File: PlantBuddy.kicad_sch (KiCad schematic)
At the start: 42 parts, among them J1 USB_C_Receptacle_USB2.0, J2 C+, J3 C-, J4 Expansion Header, Q1 DMG1012T, SW1 SW_Push, U1 LTR-303ALS-01, U2 SHTC3, U3 ESP32-S3-WROOM-1-N8R8, U4 BQ24072RGT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

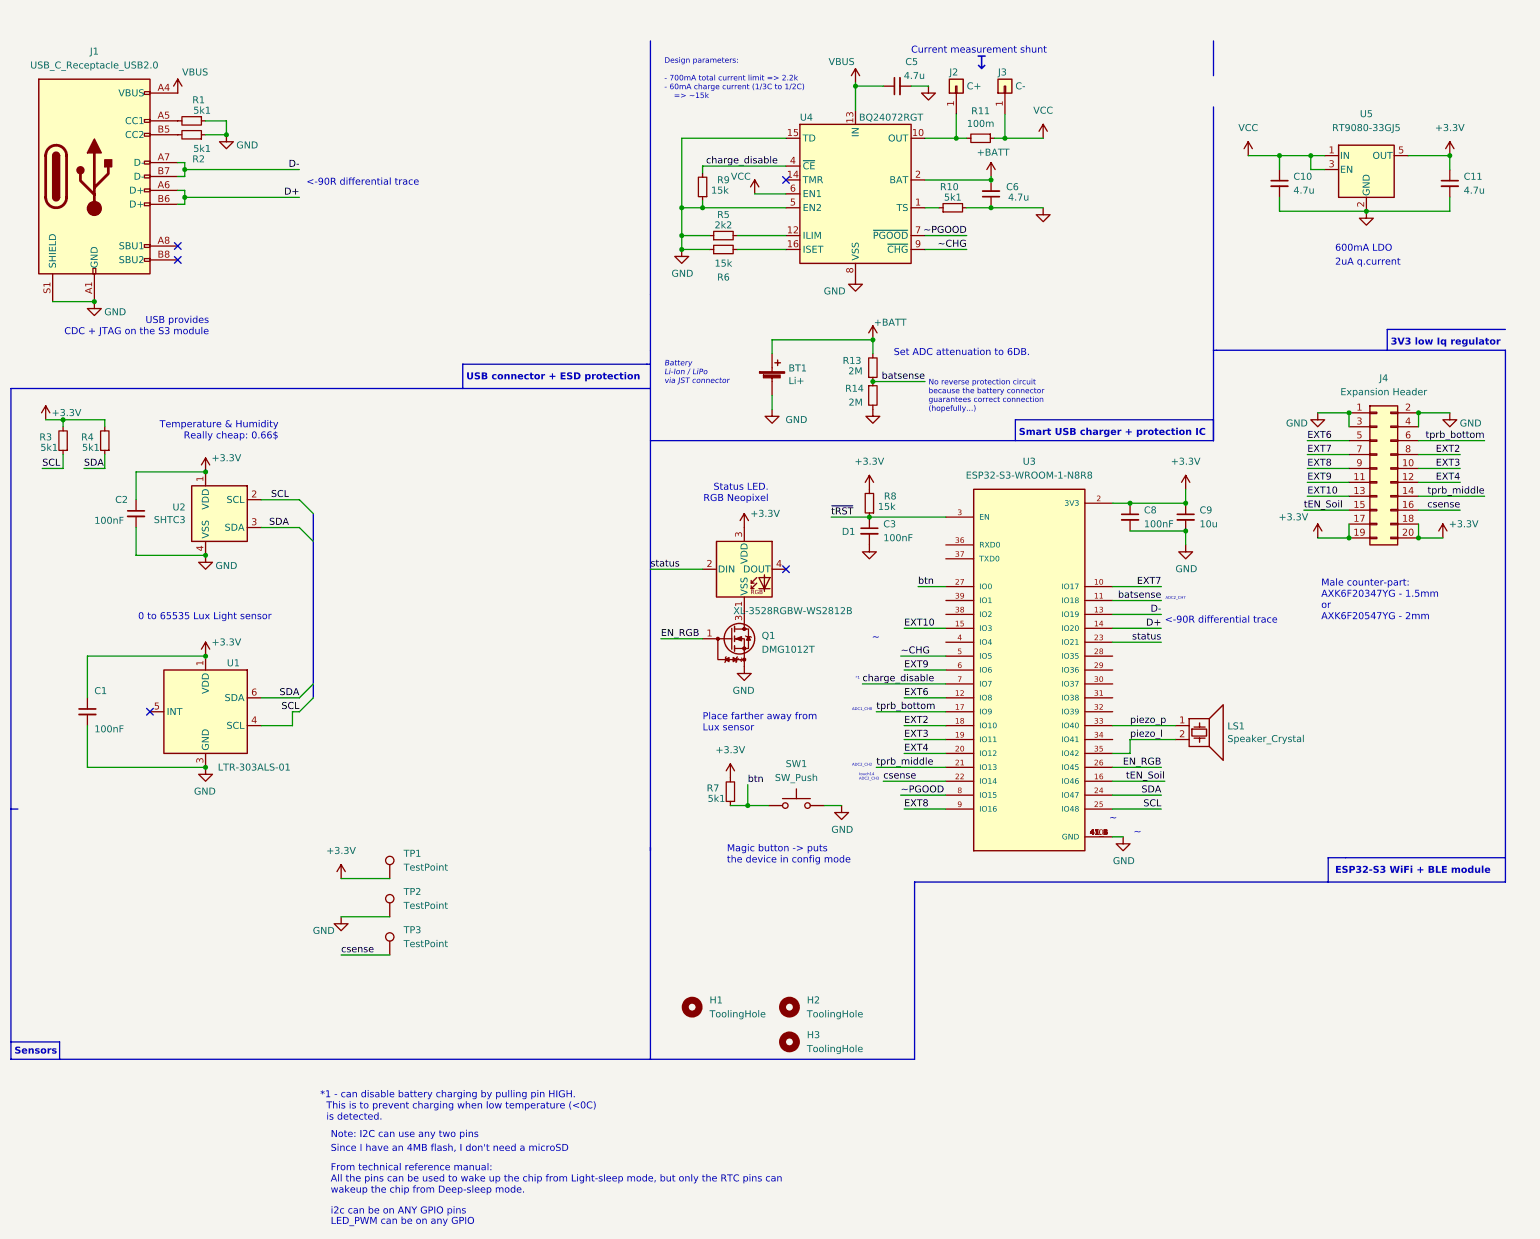
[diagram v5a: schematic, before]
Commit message: Fixed board after first batch arrived. Changed connector to FFC.
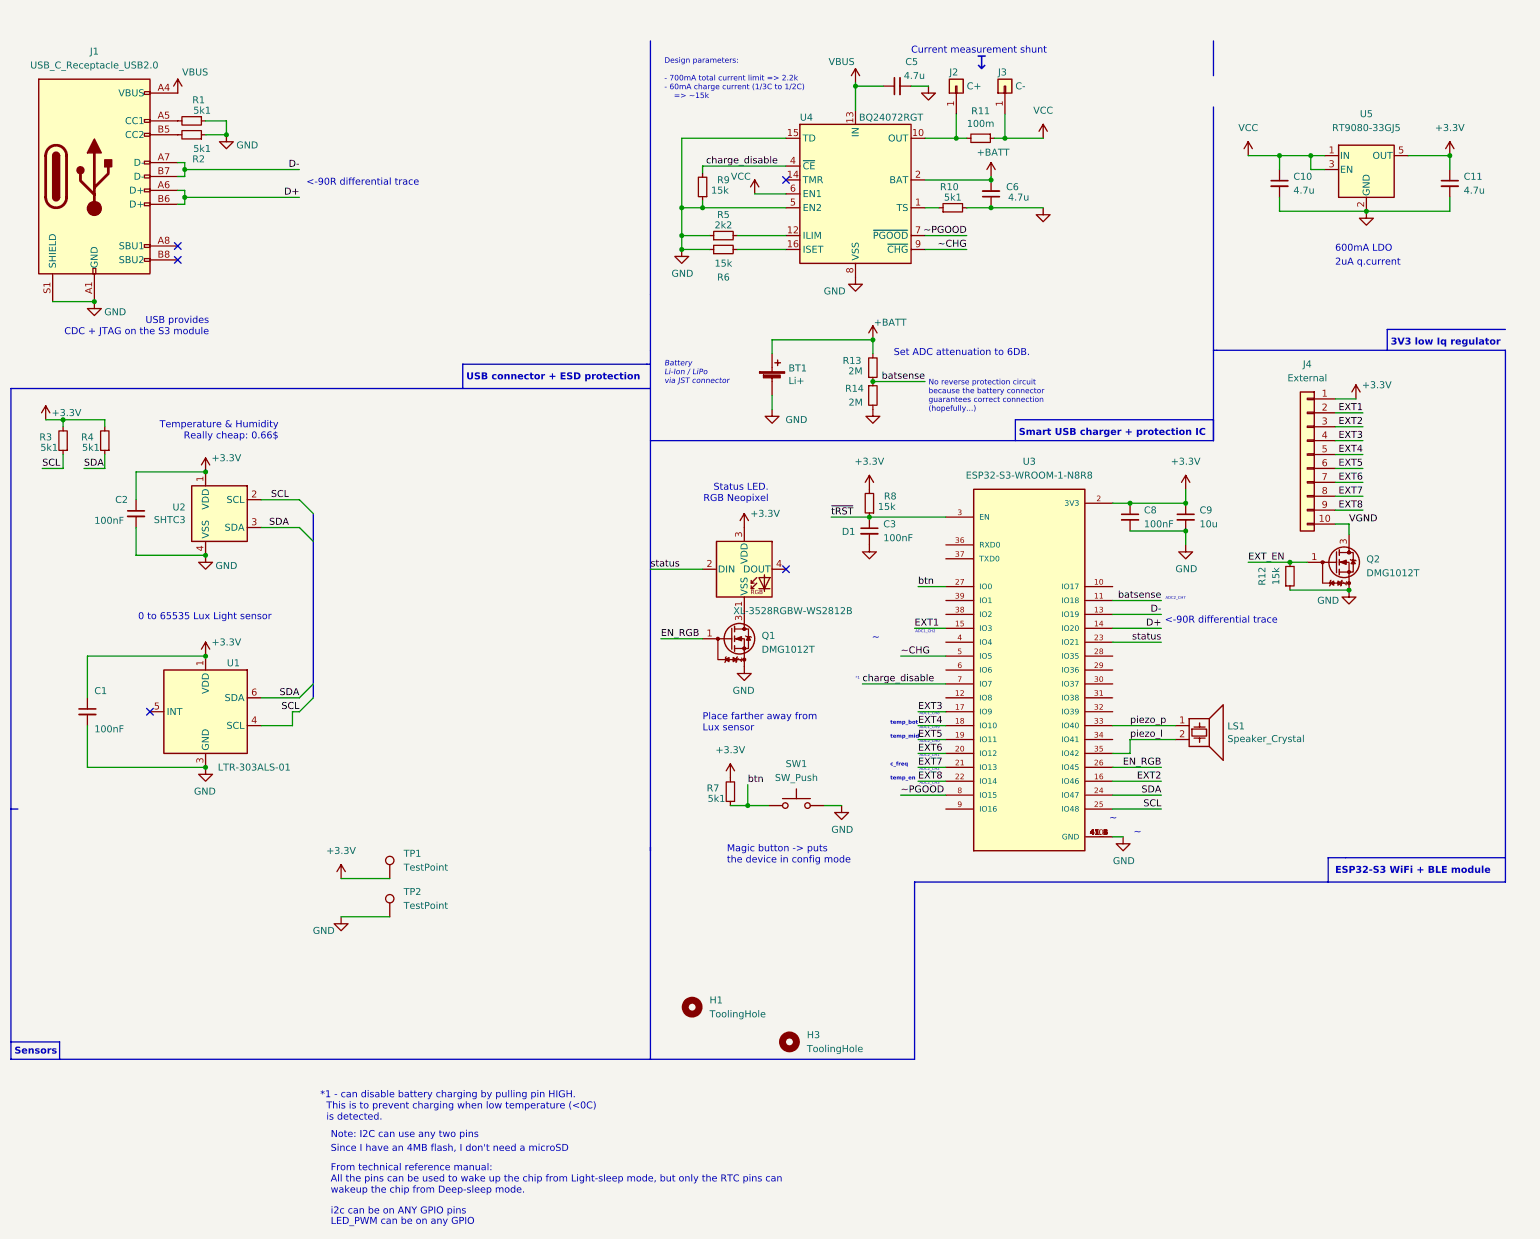
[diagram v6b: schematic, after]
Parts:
- removed H2: ToolingHole, Tooling:JLCPCB_Tooling_hole, symbol Mechanical:MountingHole
- removed J4: Expansion Header, Mezzanine-pb:AXK5F20547YG, symbol Connector_Generic:Conn_02x10_Odd_Even
- removed TP3: TestPoint, TestPoint:TestPoint_Pad_D2.0mm, symbol Connector:TestPoint
- added J4: External, Connector_FFC-FPC:Hirose_FH12-10S-0.5SH_1x10-1MP_P0.50mm_Horizontal, symbol Connector_Generic:Conn_01x10
- added Q2: DMG1012T, Package_TO_SOT_SMD:SOT-523, symbol Transistor_FET:DMG1012T
- added R12: 15k, Resistor_SMD:R_0603_1608Metric, symbol Device:R_Small
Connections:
- net csense is gone; now on net EXT8: U3.22 (IO14)
- net tEN_Soil is gone; now on net EXT2: U3.16 (IO46)
- net tprb_bottom is gone; now on net EXT3: U3.17 (IO9)
- net tprb_middle is gone; now on net EXT7: U3.21 (IO13)
- net +3V3: now also J4.1 (Pin_1)
- net EXT2: now also J4.3 (Pin_3); no longer U3.18 (IO10)
- net EXT3: now also J4.4 (Pin_4); no longer U3.19 (IO11)
- net EXT4: now also U3.18 (IO10), J4.5 (Pin_5); no longer U3.20 (IO12)
- net EXT6: now also U3.20 (IO12), J4.7 (Pin_7); no longer U3.12 (IO8)
- net EXT7: now also J4.8 (Pin_8); no longer U3.10 (IO17)
- net EXT8: now also J4.9 (Pin_9); no longer U3.9 (IO16)
- net GND: now also Q2.2 (S), R12.1
- net EXT10 renamed EXT1
- net EXT1: now also J4.2 (Pin_2)
- net EXT9: no longer names the net of U3.6 (IO6)
- new net EXT5: J4.6 (Pin_6), U3.19 (IO11)
- new net EXT_EN: Q2.1 (G), R12.2
- new net VGND: J4.10 (Pin_10), Q2.3 (D)
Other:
- note added: "ADC1_CH2"
- note added: "ADC1_CH9"
- note added: "ADC2_CH0"
- note added: "ADC2_CH1"
- note added: "ADC2_CH3"
- note added: "c_freq"
- note added: "temp_bot"
- note added: "temp_en"
- note added: "temp_mid"
- note removed: "Male counter-part: AXK6F20347YG - 1.5mm or AXK6F20547YG - 2mm"
- note removed: "touch14 ADC2_CH3"

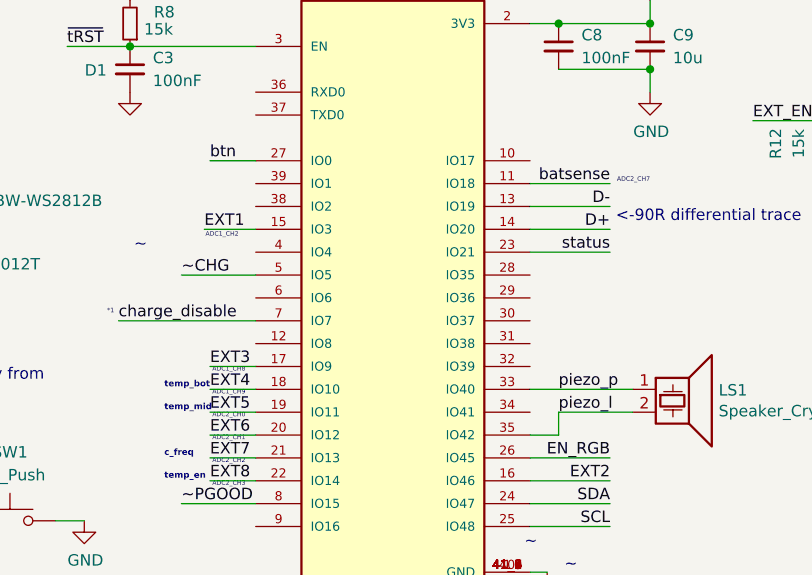
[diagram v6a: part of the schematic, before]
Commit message: Moved temp mid to ADC1_CH8 & batsense to ADC1_CH7. To note: only ADC1 can be used if WiFi is enabled!
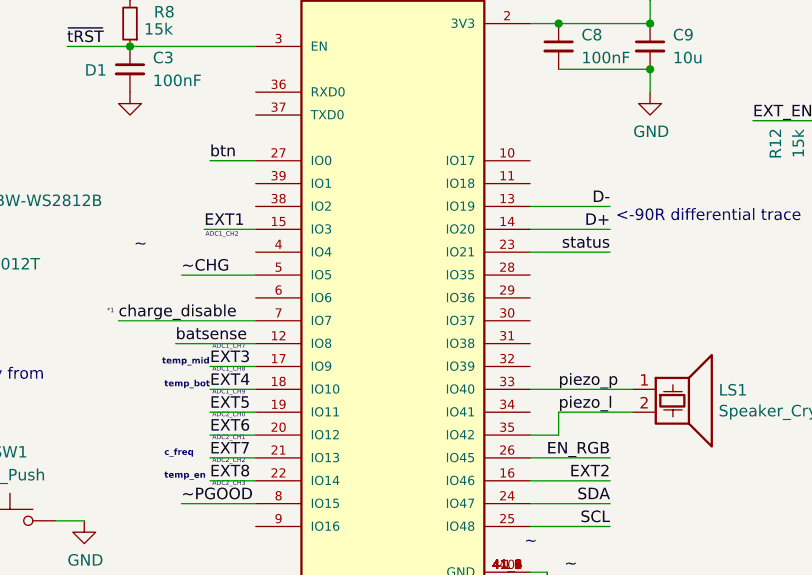
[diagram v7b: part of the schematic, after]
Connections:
- net batsense: now also U3.12 (IO8); no longer U3.11 (IO18)
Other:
- note added: "ADC1_CH7"
- note removed: "ADC2_CH7"
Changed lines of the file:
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@@
-    (stroke (width 0) (type default) (color 0 0 0 0))
-  )
-  (wire (pts (xy 222.25 114.3) (xy 213.36 114.3))
     (stroke (width 0) (type default) (color 0 0 0 0))
   )
@@
   )
   (wire (pts (xy 130.81 121.285) (xy 138.43 121.285))
+    (stroke (width 0) (type default) (color 0 0 0 0))
+  )
+  (wire (pts (xy 173.99 132.08) (xy 182.88 132.08))
     (stroke (width 0) (type default) (color 0 0 0 0))
   )
@@
   (text "i2c can be on ANY GPIO pins" (at 70.485 226.695 0)
     (effects (font (size 1.27 1.27)) (justify left bottom))
+  )
+  (text "ADC1_CH7" (at 178.054 132.842 0)
+    (effects (font (size 0.5 0.5)) (justify left bottom))
   )
   (text "From technical reference manual:\nAll the pins can be used to wake up the chip from Light-sleep mode, but only the RTC pins can\nwakeup the chip from Deep-sleep mode."
@@
     (effects (font (size 1.27 1.27)) (justify left bottom))
   )
-  (text "ADC2_CH7" (at 226.695 114.3 180)
-    (effects (font (size 0.5 0.5)) (justify right bottom))
-  )
   (text "Status LED.\nRGB Neopixel" (at 150.495 96.52 180)
     (effects (font (size 1.27 1.27)) (justify right bottom))
@@
     (effects (font (size 1 1)) (justify left bottom))
   )
-  (text "temp_mid" (at 172.72 139.7 0)
+  (text "temp_mid" (at 172.466 134.62 0)
     (effects (font (size 0.7 0.7) (thickness 0.14) bold) (justify left bottom))
   )
@@
     (effects (font (size 1.27 1.27)) (justify left bottom))
   )
+  (label "batsense" (at 173.99 132.08 0)
+    (effects (font (size 1.27 1.27)) (justify left bottom))
+  )
   (label "status" (at 222.25 121.92 180)
     (effects (font (size 1.27 1.27)) (justify right bottom))
   )
-  (label "batsense" (at 222.25 114.3 180)
-    (effects (font (size 1.27 1.27)) (justify right bottom))
-  )

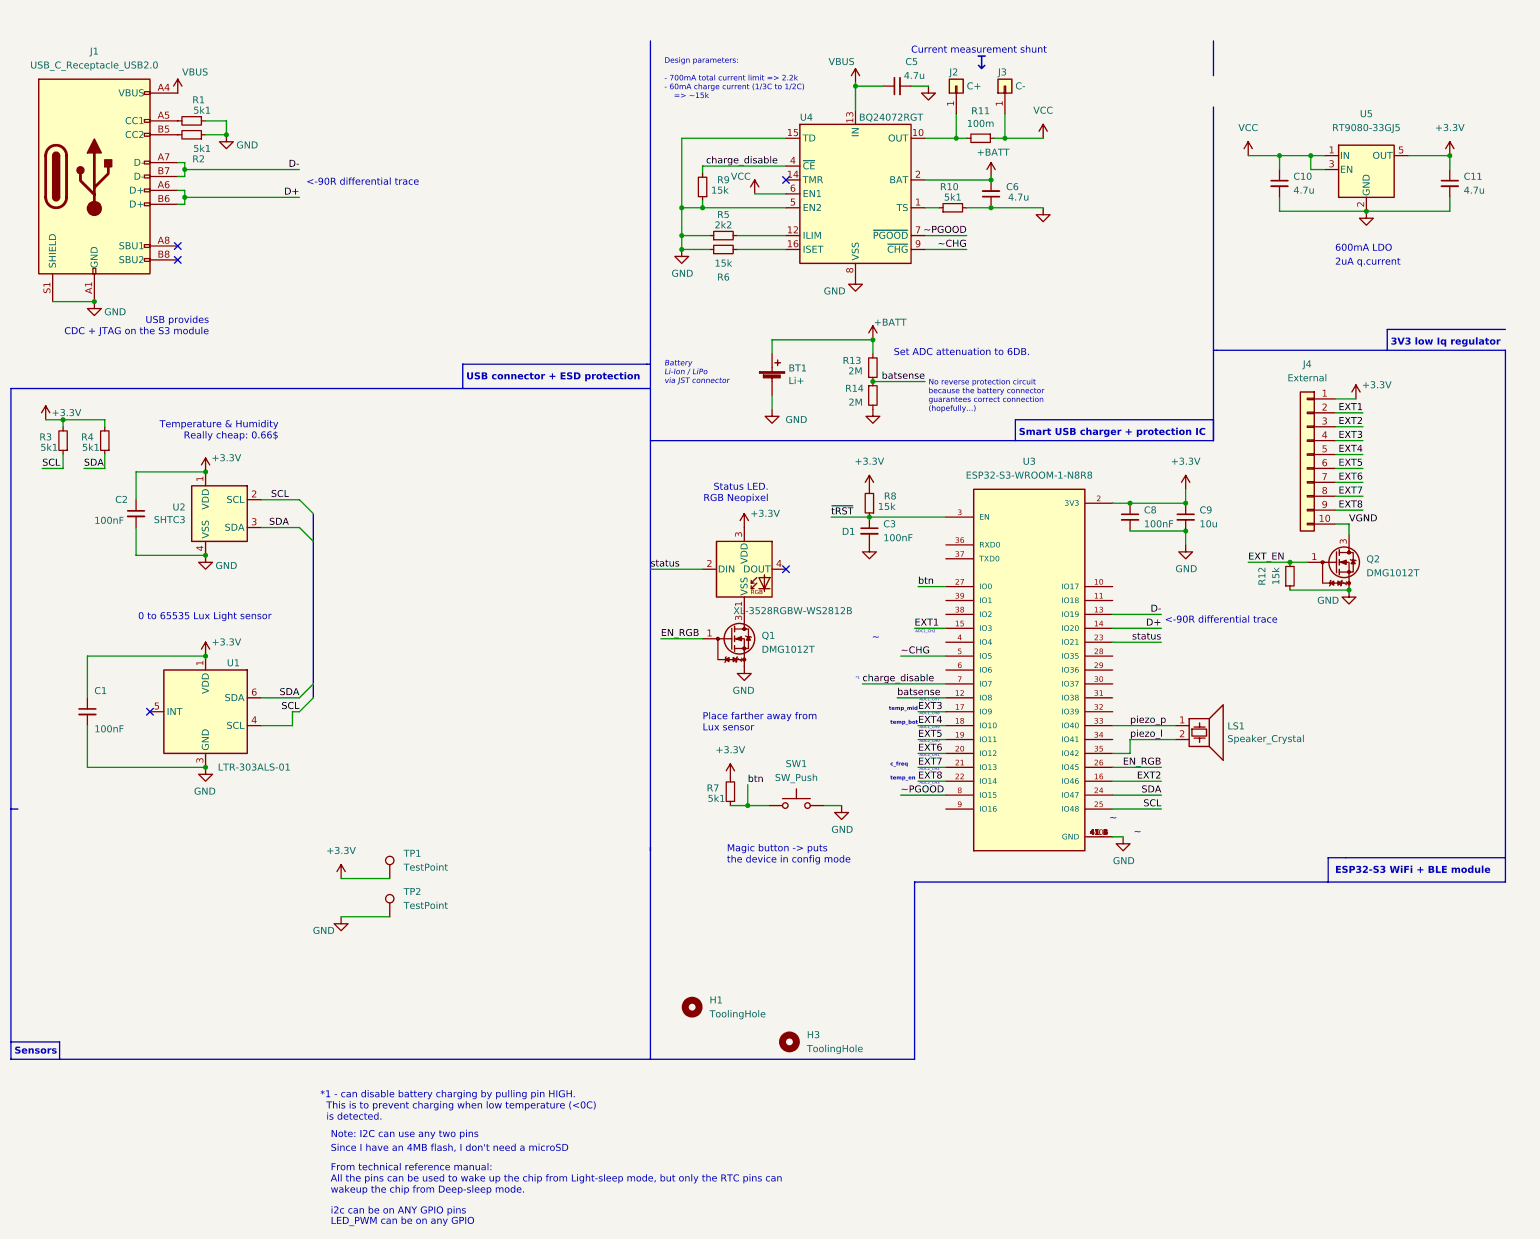
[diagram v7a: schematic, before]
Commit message: Added power distribution switch for external connector
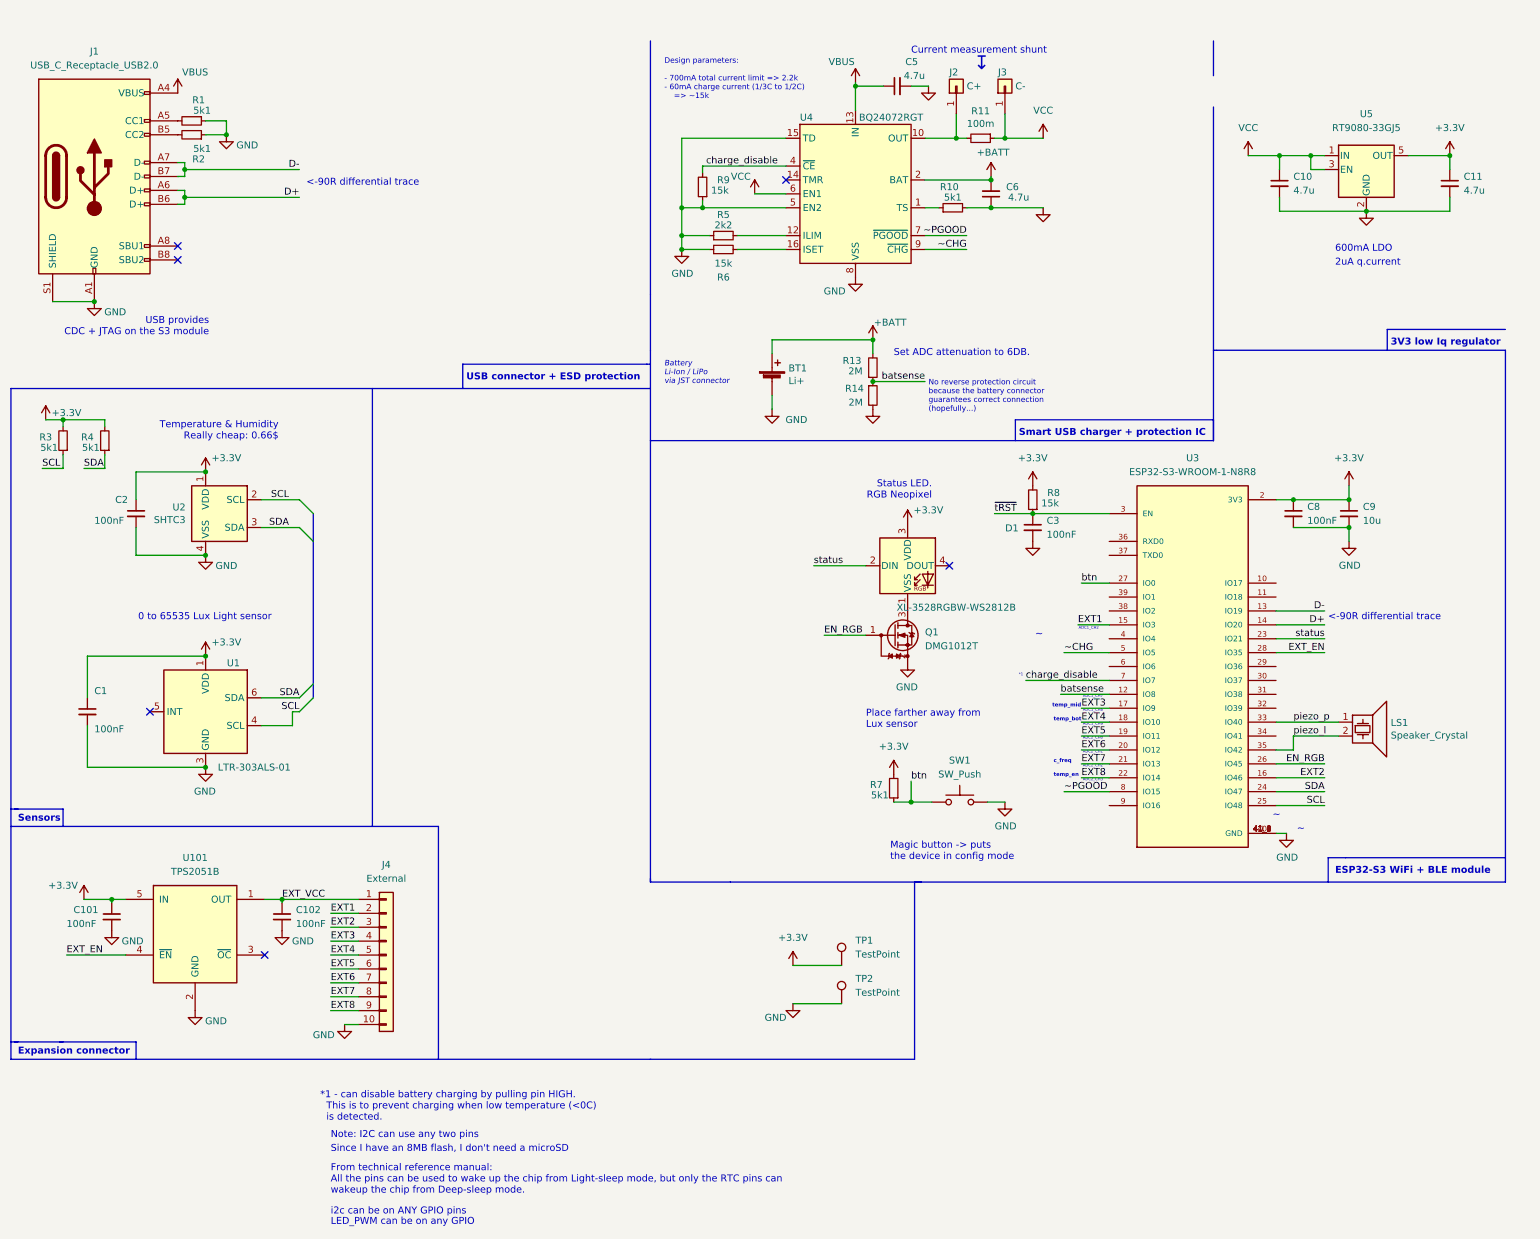
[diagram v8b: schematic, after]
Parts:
- removed H1, H3: ToolingHole, Tooling:JLCPCB_Tooling_hole, symbol Mechanical:MountingHole
- removed Q2: DMG1012T, Package_TO_SOT_SMD:SOT-523, symbol Transistor_FET:DMG1012T
- removed R12: 15k, Resistor_SMD:R_0603_1608Metric, symbol Device:R_Small
- added C101, C102: 100nF, Capacitor_SMD:C_0402_1005Metric, symbol Device:C_Small
- added U101: TPS2051B, Package_TO_SOT_SMD:SOT-23-5, symbol tps2051:TPS2051B
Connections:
- net VGND is gone; now on net GND: J4.10 (Pin_10)
- net +3V3: now also C101.1, U101.5 (IN); no longer J4.1 (Pin_1)
- net EXT_EN: now also U3.28 (IO35), U101.4 (~{EN})
- net GND: now also C101.2, C102.2, U101.2 (GND)
- new net EXT_VCC: C102.1, J4.1 (Pin_1), U101.1 (OUT)
- no-connect marks 5 -> 6
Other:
- note added: "Expansion connector"
- note added: "Since I have an 8MB flash, I don't need a microSD"
- note removed: "Since I have an 4MB flash, I don't need a microSD"
- moved on the sheet: C3, C8, C9, D1, J4, LS1, Q1, R7, R8, SW1, TP1, TP2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
